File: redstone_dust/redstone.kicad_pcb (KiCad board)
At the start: 2 copper layers, 85 x 40 mm, 74 parts, among them J1 1x4_Pogo, J2 1x4_Pogo, J3 1x4_Pogo, J4 1x4_Pogo, J5 1x4_Pogo, J6 1x4_Pogo, J7 1x4_Pogo, J8 1x4_Pogo, J9 2.54mm_ProgrammingPin, Q1 BC108, Q2 BC108, Q3 BC108, Q4 BC108, SW1 SW_Push_Open, U1 RP2040, U2 RBT05W24S05, U3 TPS62162DSG, U5 W25Q16JVSS

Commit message: add more traces, almost done
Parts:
- added C6: 0.1uF, SamacSys_Parts:CAPC2012X140N, F.Cu at (138.0, 60.8)
- added C7: 1uF, SamacSys_Parts:CAPC0603X33N, F.Cu at (139.5, 61.2)
- moved J9 46.2 mm to (121.4, 69.0), turned to 90 degrees
- moved D18 46.0 mm to (150.5, 58.0)
- moved D21 44.6 mm to (119.9, 50.5)
- moved D20 39.5 mm to (131.5, 70.5), turned to -90 degrees
- moved SW1 18.0 mm to (148.0, 70.0)
- moved Q3 12.6 mm to (129.5, 62.5), turned to -90 degrees
- moved R20 5.51 mm to (131.5, 61.7)
- moved R10 1.50 mm to (135.0, 69.0), turned to 180 degrees
- moved R11 1.50 mm to (135.0, 65.5), turned to 180 degrees
- moved R12 1.50 mm to (135.0, 62.0), turned to 180 degrees
- moved R9 1.50 mm to (135.0, 72.5), turned to 180 degrees
- moved Q2 0.78 mm to (147.2, 60.3), turned to 180 degrees
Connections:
- J9 pad 1: Net-(J9-Pin_1) -> GND
- J9 pad 4: GND -> Net-(J9-Pin_4)
- R20 pad 2: Net-(U1-GPIO16) -> Net-(U1-GPIO12)
- SW1 pad 2: Net-(J9-Pin_1) -> Net-(J9-Pin_4)
- U1 pad 11: /S_RX -> unconnected-(U1-GPIO8-Pad11)
- U1 pad 12: /S_TX -> unconnected-(U1-GPIO9-Pad12)
- U1 pad 15: unconnected-(U1-GPIO12-Pad15) -> Net-(U1-GPIO12)
- U1 pad 16: unconnected-(U1-GPIO13-Pad16) -> /S_TX
- U1 pad 17: unconnected-(U1-GPIO14-Pad17) -> /S_RX
- U1 pad 24: Net-(J9-Pin_2) -> Net-(J9-Pin_3)
- U1 pad 25: Net-(J9-Pin_3) -> Net-(J9-Pin_2)
- U1 pad 26: Net-(J9-Pin_1) -> Net-(J9-Pin_4)
- U1 pad 27: Net-(U1-GPIO16) -> unconnected-(U1-GPIO16-Pad27)
- U1 pad 29: unconnected-(U1-GPIO18-Pad29) -> /E_RX
- U1 pad 30: unconnected-(U1-GPIO19-Pad30) -> /E_TX
- U1 pad 31: /E_RX -> unconnected-(U1-GPIO20-Pad31)
- U1 pad 32: /E_TX -> unconnected-(U1-GPIO21-Pad32)
- U1 pad 36: /N_RX -> /N_TX
- U1 pad 37: /N_TX -> /N_RX
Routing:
- net /S_TX: track 0.00 -> 33.7 mm, vias 0 -> 1
- net Net-(J9-Pin_4): track 0.00 -> 30.8 mm, vias 0 -> 1
- net /S_RX: track 0.00 -> 26.2 mm, vias 0 -> 2
- net /E_TX: track 13.3 -> 36.1 mm, vias 0 -> 2
- net /3.3V_LOCAL: track 43.5 -> 65.6 mm
- net Net-(J9-Pin_2): track 0.00 -> 19.1 mm, vias 0 -> 1
- net /W_TX: track 11.6 -> 28.4 mm
- net /E_RX: track 12.4 -> 28.6 mm, vias 0 -> 1
- net Net-(J9-Pin_3): track 0.00 -> 15.8 mm, vias 0 -> 1
- net /W_RX: track 10.9 -> 21.9 mm
- net /N_TX: track 30.2 -> 39.2 mm
- net /N_RX: track 23.6 -> 32.1 mm
- net Net-(D5-K): track 13.3 -> 15.9 mm
- net Net-(U1-GPIO16): track 2.47 -> 0.00 mm, vias 1 -> 0
- net Net-(Q2-B): track 6.11 -> 3.66 mm
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
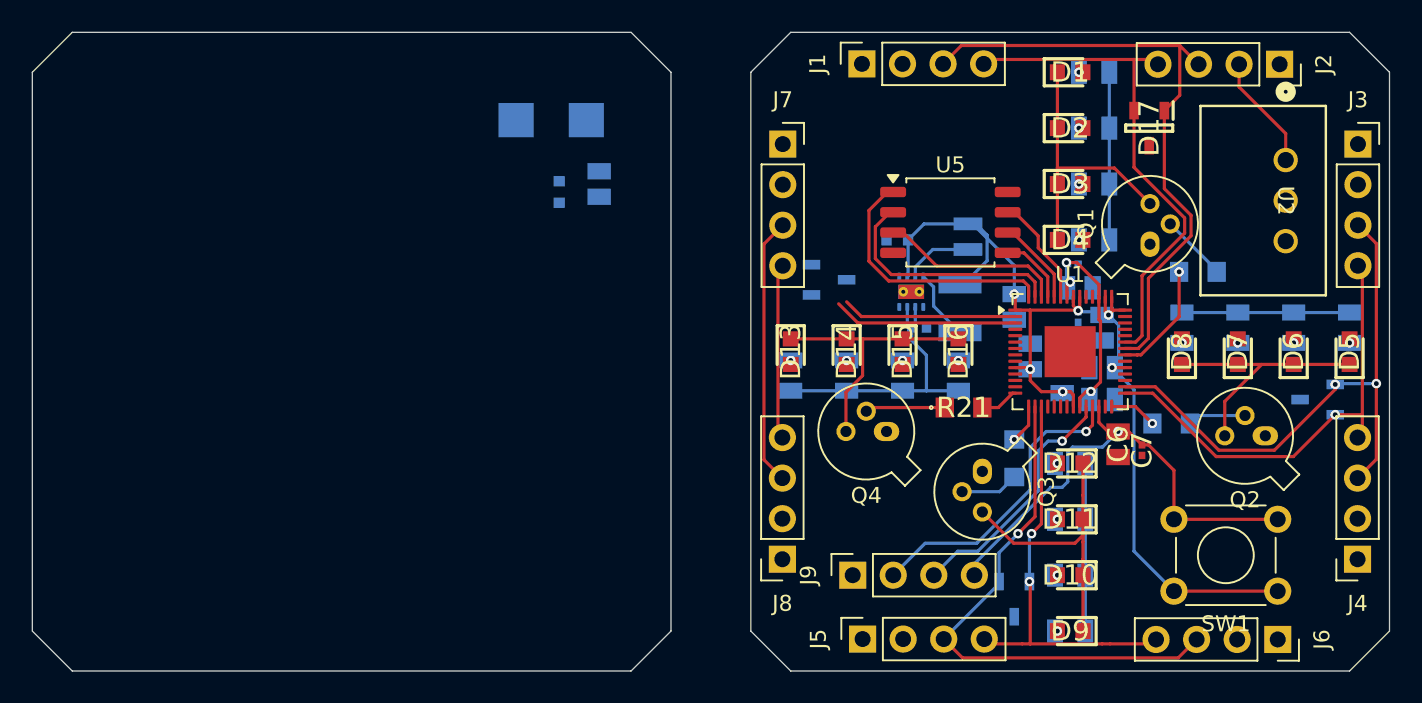
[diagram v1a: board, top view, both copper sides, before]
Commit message: add remaining tracks except ground
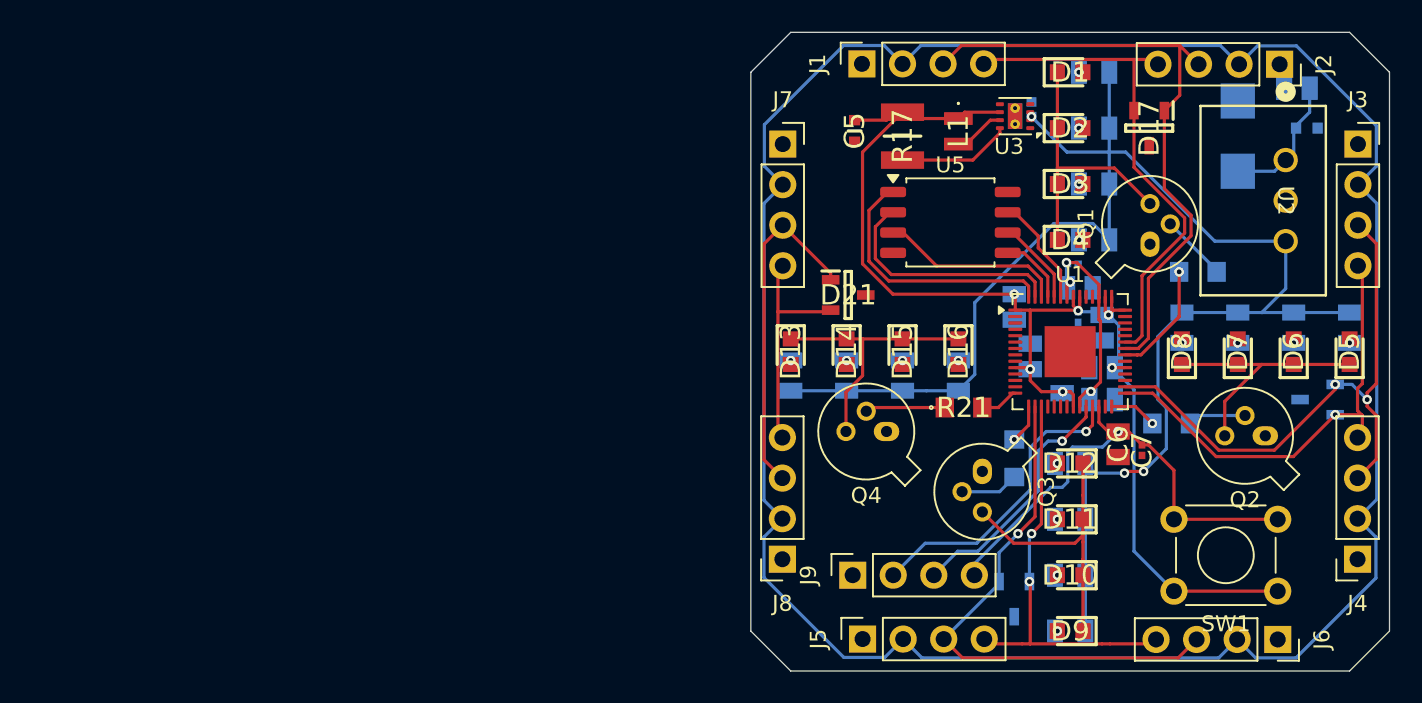
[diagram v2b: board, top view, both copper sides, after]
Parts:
- C5, D21, L1, R17, U3: moved to F.Cu
- moved C4 47.0 mm to (149.8, 41.0), turned to 0 degrees
- moved C3 44.1 mm to (149.2, 38.5), turned to 180 degrees
- moved D19 43.0 mm to (145.5, 41.5), turned to 90 degrees
- moved C1 15.4 mm to (132.6, 39.8), turned to 90 degrees
- moved U3 12.8 mm to (131.6, 40.2), turned to 180 degrees
- moved R17 11.4 mm to (124.5, 41.5)
- moved C5 7.33 mm to (121.5, 41.2), turned to -90 degrees
- moved L1 6.63 mm to (128.0, 41.2)
- moved D21 1.53 mm to (121.1, 51.5)
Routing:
- net VCC: track 7.21 -> 157.9 mm
- net /5V_LOCAL: track 49.1 -> 99.2 mm, vias 0 -> 3
- net /3.3V_LOCAL: track 65.6 -> 78.4 mm
- net /W_RX: track 21.9 -> 14.3 mm
- net /W_TX: track 28.4 -> 21.5 mm
- net Net-(U3-PG): track 4.45 -> 7.11 mm
- net Net-(U3-SW): track 4.36 -> 3.22 mm
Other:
- board size 85 x 40 mm -> 40 x 40 mm

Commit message: move pins closer to the corners, create ground plane fill on bottom
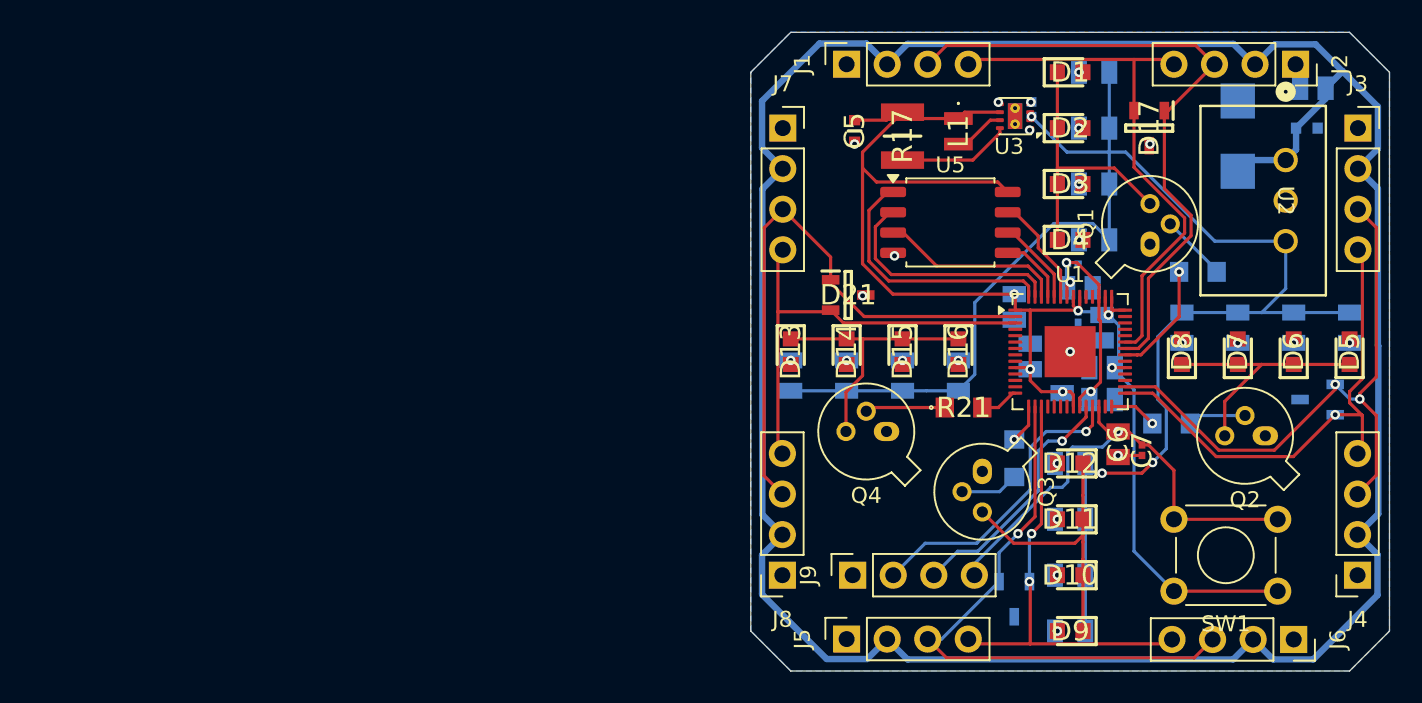
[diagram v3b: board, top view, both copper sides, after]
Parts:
- moved C3 1.00 mm to (150.2, 38.5)
- moved J2 1.00 mm to (149.1, 37.0)
- moved J3 1.00 mm to (153.0, 41.0)
- moved J4 1.00 mm to (153.0, 69.0)
- moved J5 1.00 mm to (121.0, 73.0)
- moved J6 1.00 mm to (149.0, 73.0)
- moved J7 1.00 mm to (117.0, 41.0)
- moved J8 1.00 mm to (117.0, 69.0)
- moved J1 0.96 mm to (121.0, 37.0)
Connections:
- U1 pad 2: /W_RX -> /W_TX
- U1 pad 3: /W_TX -> /W_RX
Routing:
- net /W_TX: track 21.5 -> 37.1 mm
- net /W_RX: track 14.3 -> 28.2 mm
- net /3.3V_LOCAL: track 78.4 -> 88.1 mm
- net VCC: track 157.9 -> 163.8 mm
- net /S_TX: track 33.7 -> 36.7 mm
- net GND: track 0.00 -> 2.81 mm, vias 0 -> 9
- net /E_RX: track 28.9 -> 31.3 mm
- net /S_RX: track 26.2 -> 28.2 mm
- net /N_RX: track 32.1 -> 34.1 mm
- net /E_TX: track 36.4 -> 38.4 mm
- net /N_TX: track 39.2 -> 41.1 mm
- added copper zone on B.Cu, net GND

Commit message: reasolve all drc check errors, todo resolve warnings
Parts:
- moved C4 2.59 mm to (150.5, 43.5), turned to -90 degrees
- moved C3 2.24 mm to (149.2, 40.5), turned to 0 degrees
- moved Q1 1.20 mm to (140.7, 47.3), turned to 135 degrees
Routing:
- net GND: track 2.81 -> 19.3 mm, vias 9 -> 18
- net VCC: track 163.8 -> 173.7 mm
- net /5V_LOCAL: track 99.2 -> 103.9 mm, vias 3 -> 9
- net Net-(Q1-B): track 4.20 -> 5.94 mm
- net /E_TX: track 38.4 -> 38.2 mm, vias 2 -> 1
- net /S_TX: vias 1 -> 2

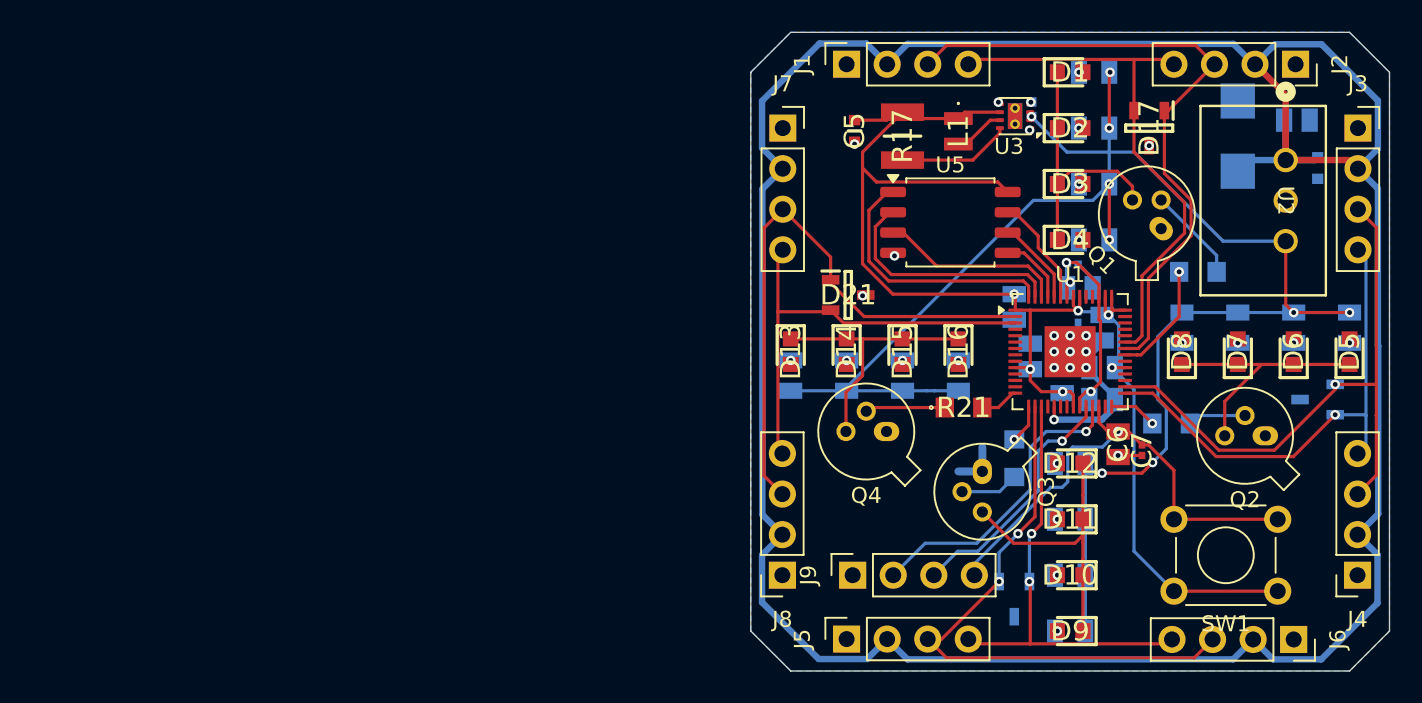
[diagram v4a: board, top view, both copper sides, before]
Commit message: fix front side silkscreens
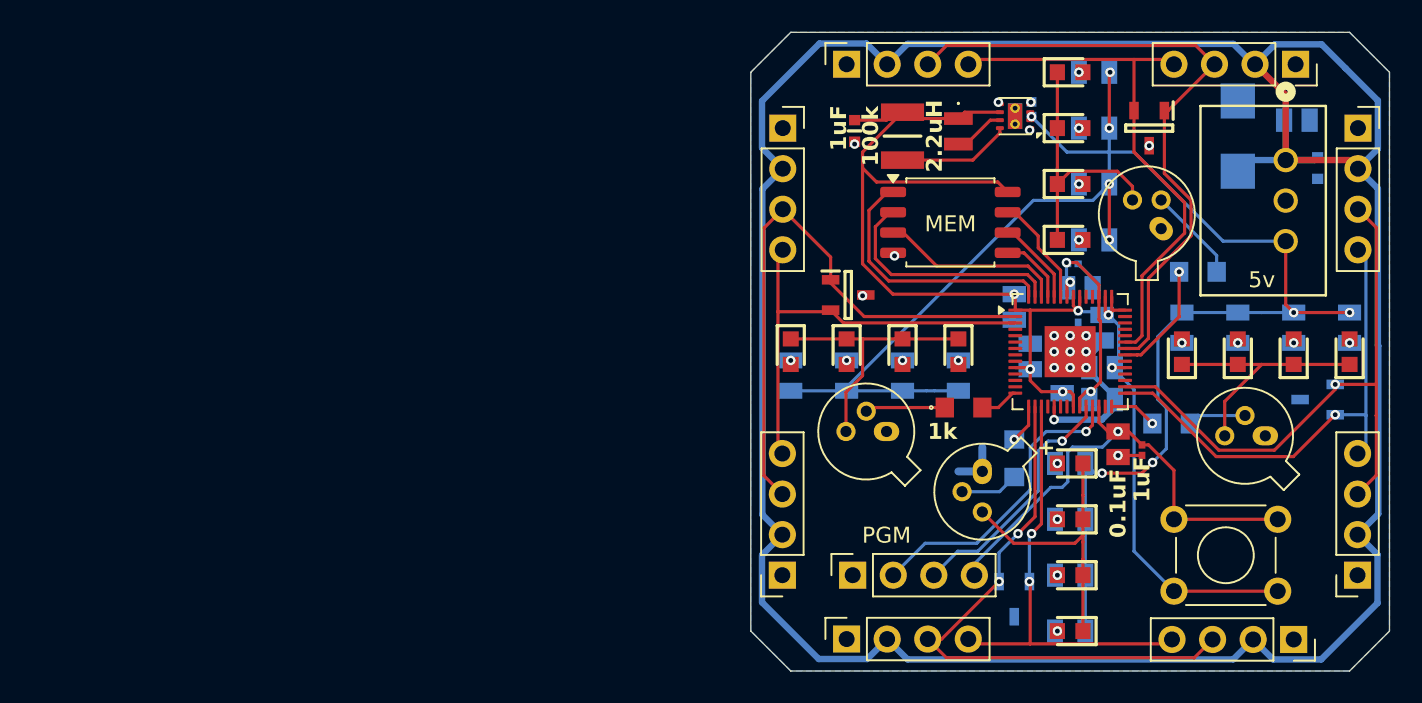
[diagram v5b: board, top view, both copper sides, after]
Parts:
- + LED -: renamed from D9
- - LED +: renamed from D5
- renumbered C6 to 0.1uF, C2 to 0.1uF, C3 to 0.1uF, R17 to 100k, C1 to 10uF, R21 to 1k, R18 to 1k, R19 to 1k, R20 to 1k, C7 to 1uF, C5 to 1uF, L1 to 2.2uH, R15 to 200, R11 to 200, R6 to 200, R1 to 200, C4 to 22uF, U3 to 3.3v, U2 to 5v, Q2 to BC108, Q1 to BC108, Q3 to BC108, Q4 to BC108, U5 to MEM, J9 to PGM, D19 to TVS
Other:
- board text added: "+"
